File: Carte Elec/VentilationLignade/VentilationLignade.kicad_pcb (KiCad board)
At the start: 2 copper layers, 65 parts, among them P1 RelaisBoard1, P10 SDCard, P11 Codeur Rotatif, P12 Teensy Bottom, P13 EndStops1, P14 Teensy_Haut, P15 EndStops2, P16 Teensy_cote, P17 Retour 12V, P18 Masse_12V, P19 12V1, P2 Temp_Ext, P20 12V2, P21 12V_1et2, P22 Teensy_Bas, P23 Serial, P24 Temp_PuitC, P3 RelaisBoard2, P4 Temp_Int, P5 RelaisBoard3, P6 Temp_Chem, P7 RelaisBoard4, P8 RelaisBoard5, P9 TFT, SW1 Reset_Push, SW2 BackLight_On/ff, U2 OPTO-TRANSISTOR, U3 OPTO-TRANSISTOR, U4 OPTO-TRANSISTOR, U5 OPTO-TRANSISTOR, U6 OPTO-TRANSISTOR

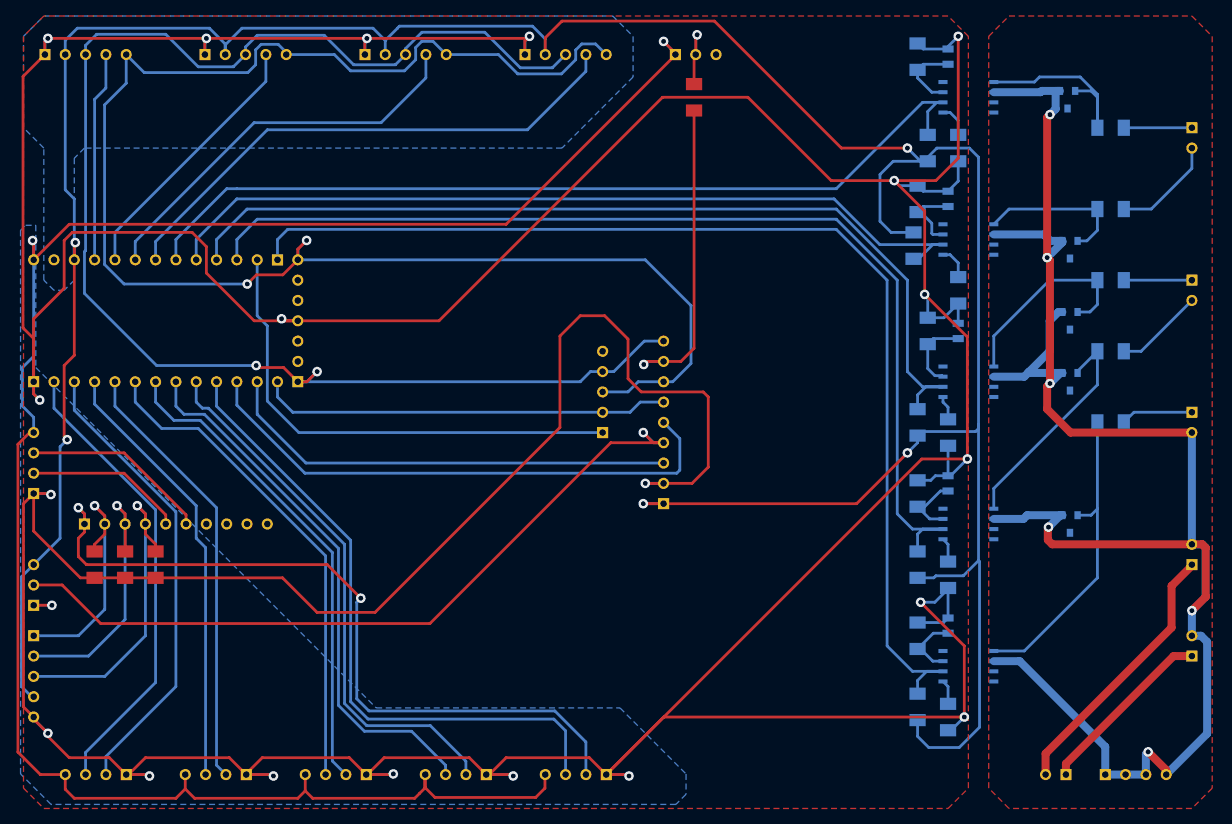
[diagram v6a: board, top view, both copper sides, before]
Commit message: Agrandissement des pads de connecteur, pour pouvoir percer et souder sans soucis.
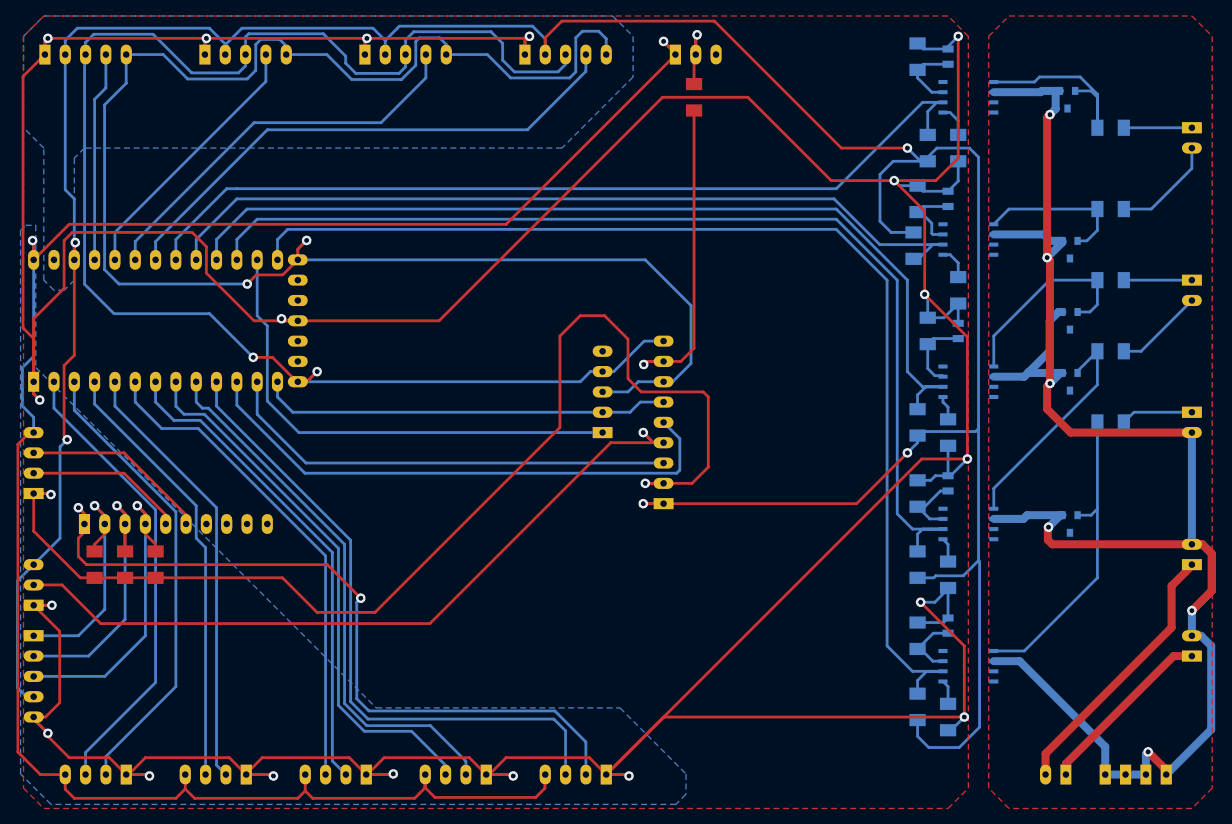
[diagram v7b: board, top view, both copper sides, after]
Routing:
- net GND: track 815.9 -> 804.5 mm
- net SPI_SCK: track 202.8 -> 213.1 mm
- net SPI_MISO: track 186.6 -> 193.9 mm
- net GNDPWR: track 224.3 -> 226.0 mm
- net +3.3V: track 385.1 -> 385.9 mm

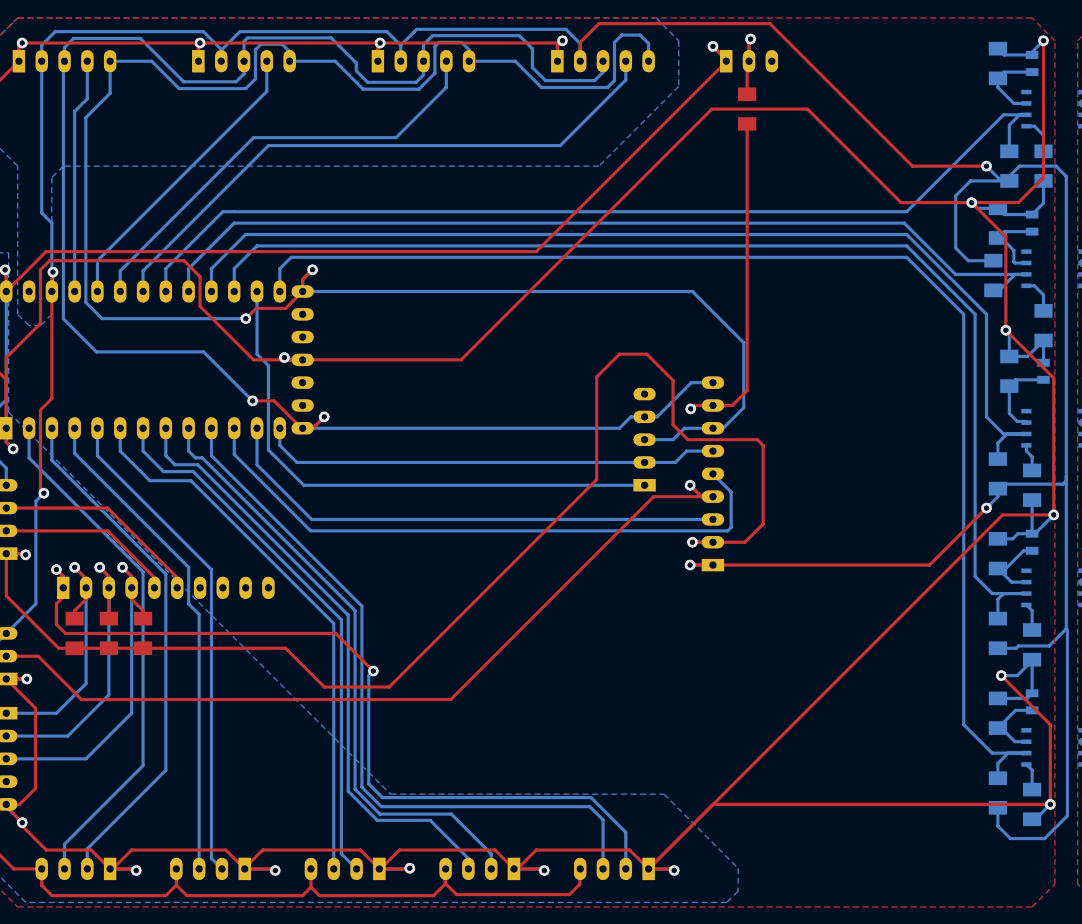
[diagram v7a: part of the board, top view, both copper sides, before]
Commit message: Eloignement des pistes proches
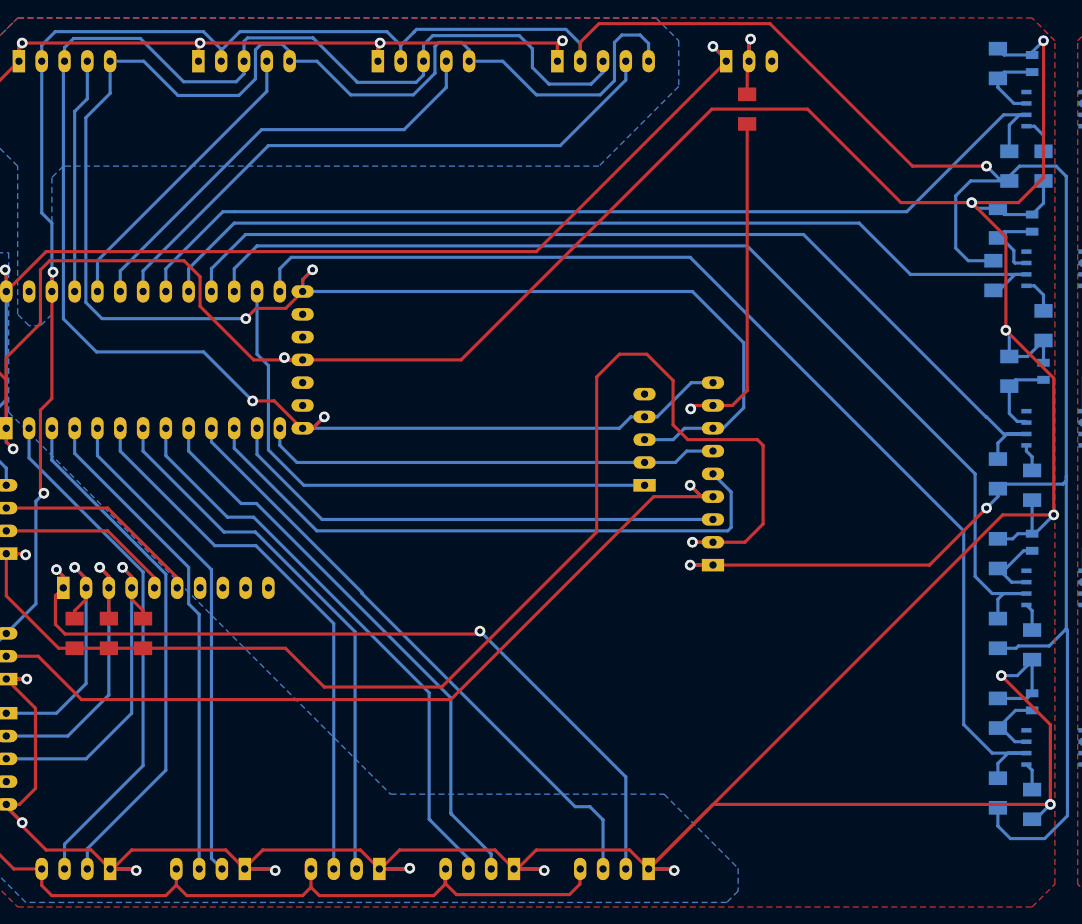
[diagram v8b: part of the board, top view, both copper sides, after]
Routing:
- net 12V_CHECK: track 141.2 -> 127.1 mm
- net 12V2_ON: track 80.8 -> 68.1 mm
- net ENDSTOP_2_2: track 130.6 -> 120.2 mm
- net ENDSTOP_2_1: track 116.2 -> 109.6 mm
- net SELECT_VMC: track 68.2 -> 64.1 mm
- net SELECT_12V: track 94.3 -> 90.2 mm
- net GND: track 804.5 -> 807.9 mm
- net 12V1_ON: track 68.0 -> 64.8 mm
- net SPI_SCK: track 213.1 -> 215.0 mm
- net TFT_CS: track 57.4 -> 56.7 mm
